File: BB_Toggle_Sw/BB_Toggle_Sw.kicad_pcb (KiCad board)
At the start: 2 copper layers, 18 x 13.5 mm, 3 parts, among them J1 Conn_01x03_PinHeader, J2 Conn_01x03_PinHeader, SW1 SW_DPDT_OnOffOn

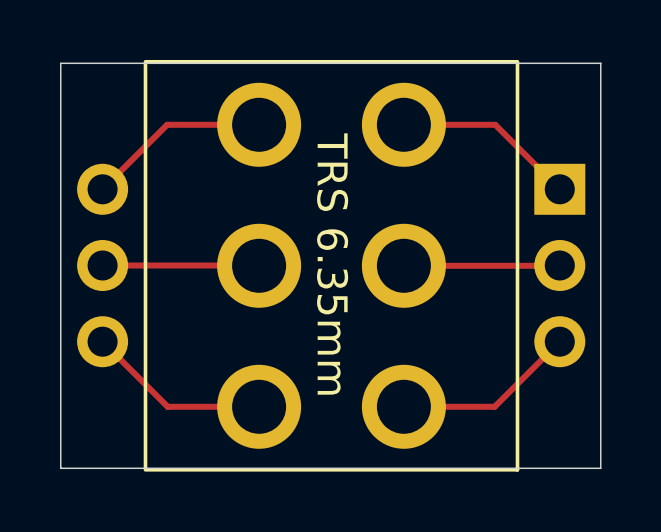
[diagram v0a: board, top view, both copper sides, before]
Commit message: Corrected text on Toggle Sw BB
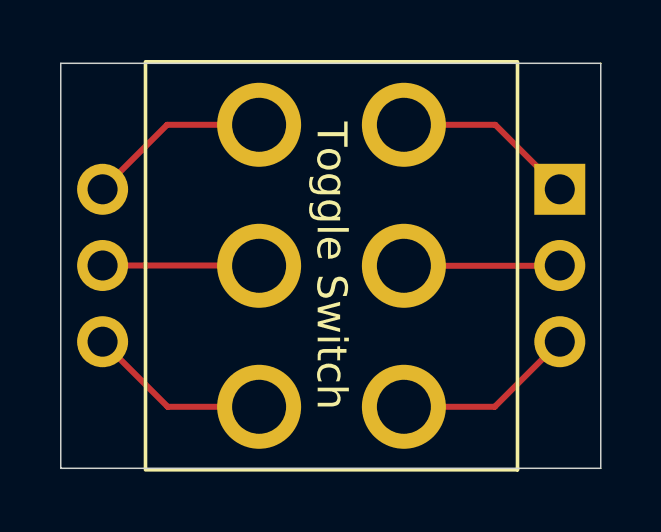
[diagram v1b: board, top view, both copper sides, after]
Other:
- board text added: "Toggle Switch"
- board text removed: "TRS 6.35mm"
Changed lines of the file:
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@@
 		(layer "Edge.Cuts")
 	)
-	(gr_text "TRS 6.35mm"
+	(gr_text "Toggle Switch"
 		(at 52.55 32.55 270)
 		(layer "F.SilkS")
@@
 			)
 		)
-	)
-	(segment
-		(start 54.963 37.25)
-		(end 57.99 37.25)
-		(width 0.2)
-		(layer "F.Cu")
-		(net "Net-(J1C-Pin_3)")
-	)
-	(segment
-		(start 57.99 37.25)
-		(end 60.16 35.08)
-		(width 0.2)
-		(layer "F.Cu")
-		(net "Net-(J1C-Pin_3)")
 	)
 	(segment
@@
 	)
 	(segment
+		(start 54.963 37.25)
+		(end 57.99 37.25)
+		(width 0.2)
+		(layer "F.Cu")
+		(net "Net-(J1C-Pin_3)")
+	)
+	(segment
+		(start 57.99 37.25)
+		(end 60.16 35.08)
+		(width 0.2)
+		(layer "F.Cu")
+		(net "Net-(J1C-Pin_3)")
+	)
+	(segment
 		(start 44.92 30)
 		(end 47.07 27.85)
@@
 		(layer "F.Cu")
 		(net "Net-(J2A-Pin_1)")
+	)
+	(segment
+		(start 50.127 32.54)
+		(end 50.137 32.55)
+		(width 0.2)
+		(layer "F.Cu")
+		(net "Net-(J2B-Pin_2)")
+	)
+	(segment
+		(start 44.92 32.54)
+		(end 50.127 32.54)
+		(width 0.2)
+		(layer "F.Cu")
+		(net "Net-(J2B-Pin_2)")
 	)
 	(segment
@@
 		(net "Net-(J2C-Pin_3)")
 	)
-	(segment
-		(start 50.127 32.54)
-		(end 50.137 32.55)
-		(width 0.2)
-		(layer "F.Cu")
-		(net "Net-(J2B-Pin_2)")
-	)
-	(segment
-		(start 44.92 32.54)
-		(end 50.127 32.54)
-		(width 0.2)
-		(layer "F.Cu")
-		(net "Net-(J2B-Pin_2)")
-	)
 	(embedded_fonts no)
